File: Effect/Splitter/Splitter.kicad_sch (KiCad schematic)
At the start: 12 parts, among them J1 Conn_01x04_Pin, J2 AudioJack2_Ground, J3 Conn_01x03_Pin, U1 OPA1655

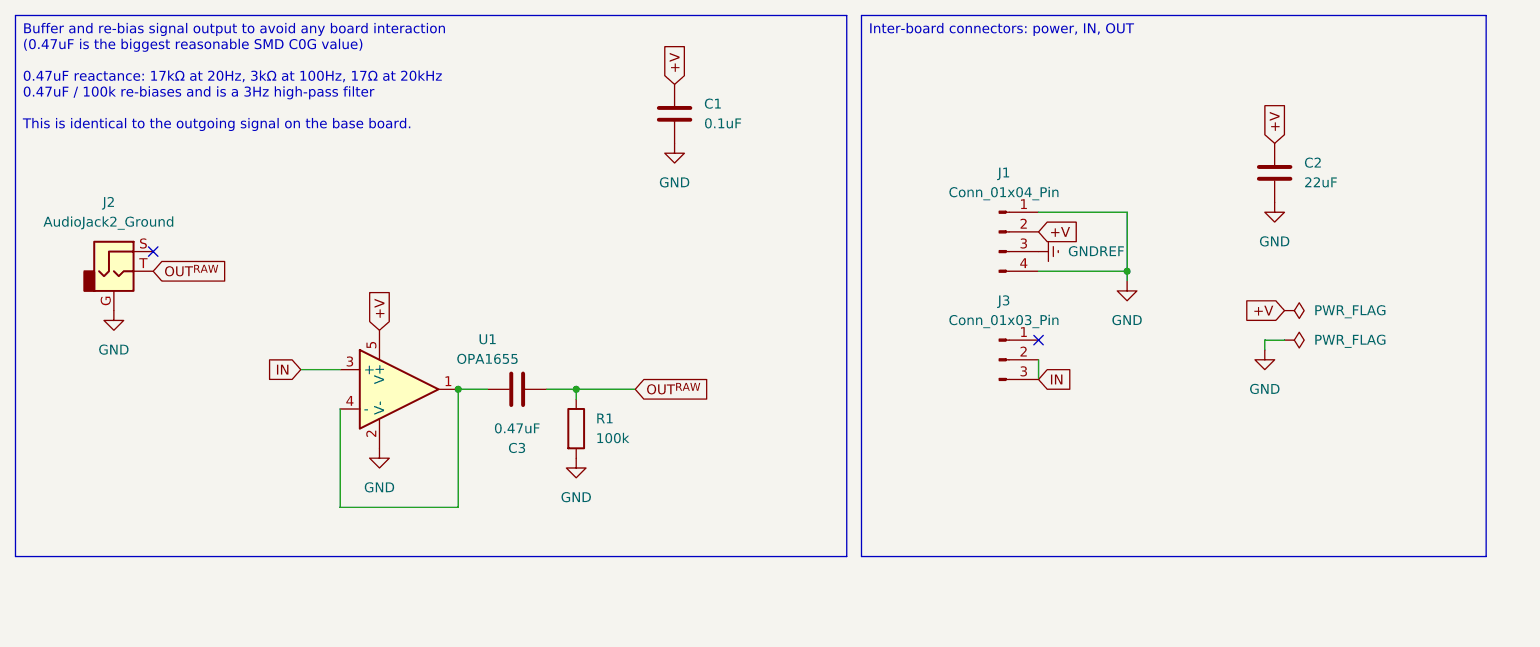
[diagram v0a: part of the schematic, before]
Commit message: Add volume control to 'splitter' board
Also stop being silly: this board needs no active circuitry.  The
incoming signal already comes from an op amp buffer on the base board,
there's no need to add a second one.

So remove the pointless op-amp, and replace the 100k resistor to ground
that is part of the signal rebiasing with a potentiometer for volume
control.

Signed-off-by: Linus Torvalds <torvalds@linux-foundation.org>
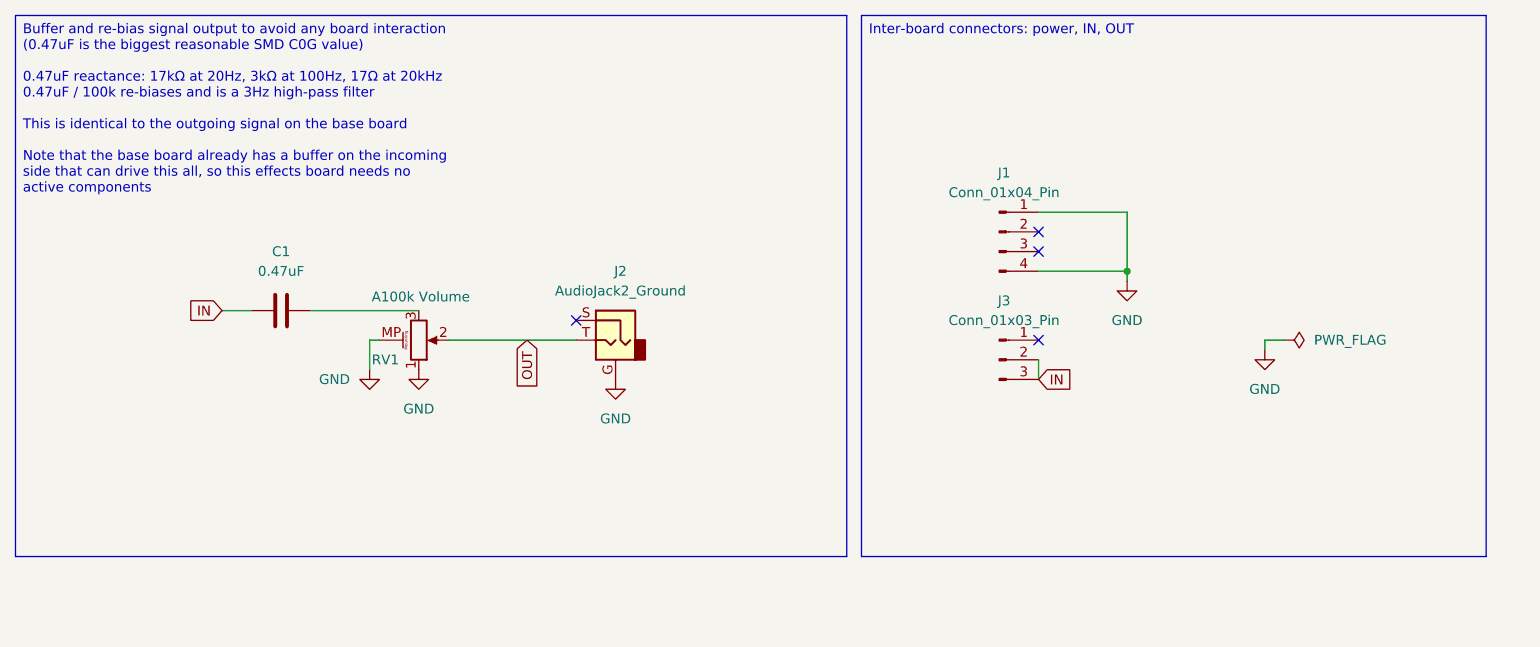
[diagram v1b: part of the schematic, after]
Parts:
- removed C1: 0.1uF, Mylib:C_0704_1810Metric, symbol Device:C
- removed C2: 22uF, Capacitor_SMD:C_1206_3216Metric_Pad1.33x1.80mm_HandSolder, symbol Device:C
- removed R1: 100k, Resistor_SMD:R_0805_2012Metric_Pad1.20x1.40mm_HandSolder, symbol Device:R
- removed U1: OPA1655, Package_TO_SOT_SMD:SOT-23-5, symbol Mylib:OPA1655DVB
- added RV1: A100k Volume, Mylib:Potentiometer_9mm_MP, symbol Device:R_Potentiometer_MountingPin
- renumbered C3 to C1
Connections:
- net +V: no longer J1.2 (Pin_2)
- net GND: now also RV1.1, RV1.MP (MountPin)
- net GNDREF: no longer J1.3 (Pin_3)
- net IN: now also C1.2
- net OUT^{RAW}: no longer names the net of C1.1
- net OUT^{RAW}: now also RV1.3; no longer J2.T
- new net OUT: J2.T, RV1.2
- no-connect marks 2 -> 4
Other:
- moved on the sheet: C1, J2
